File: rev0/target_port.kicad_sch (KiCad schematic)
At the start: 14 parts, among them IC1 ECP5-BGA256, U9 USB3343-CP

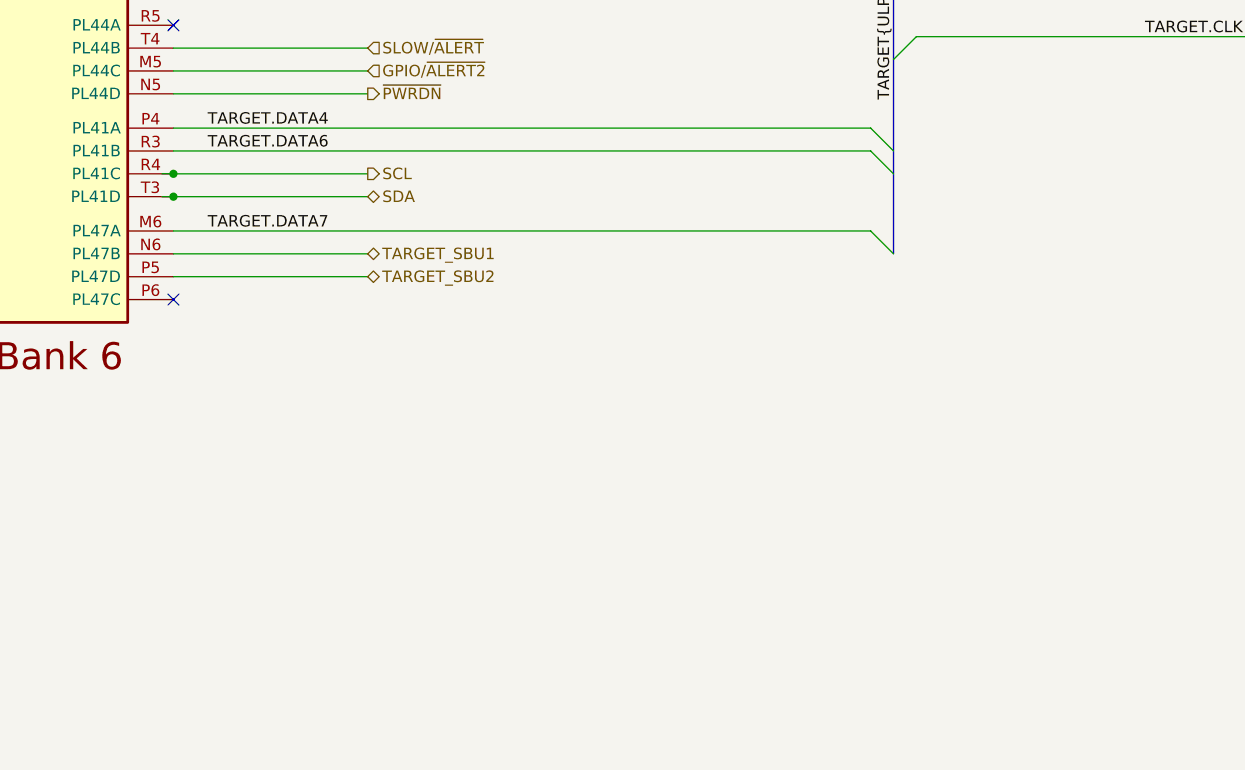
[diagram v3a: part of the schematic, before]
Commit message: hardware: add Target port Type-C controller
replaces buffers for CC pin I/O
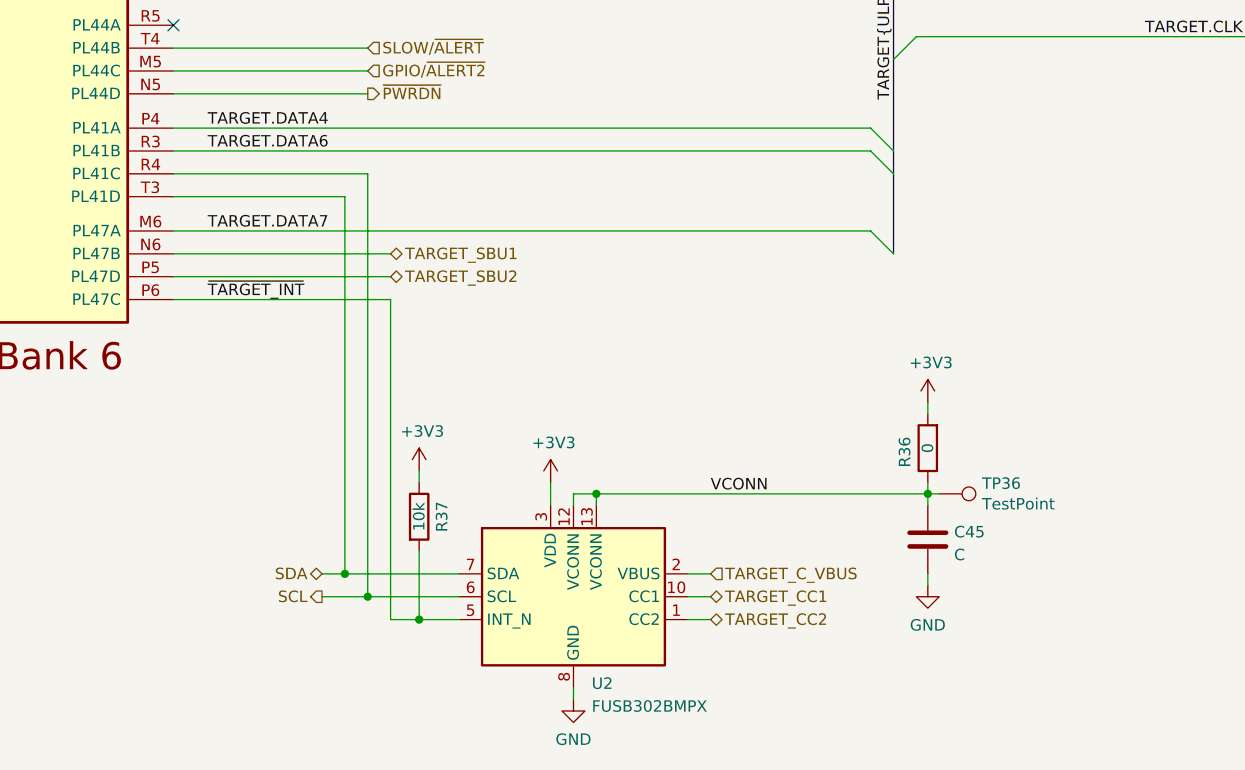
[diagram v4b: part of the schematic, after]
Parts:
- added C45: C, Capacitor_SMD:C_0402_1005Metric, symbol Device:C
- added R36: 0, Resistor_SMD:R_0402_1005Metric, symbol Device:R
- added R37: 10k, Resistor_SMD:R_0402_1005Metric, symbol Device:R
- added TP36: TestPoint, TestPoint:TestPoint_Pad_D1.0mm, symbol Connector:TestPoint
- added U2: FUSB302BMPX, Package_DFN_QFN:WQFN-14-1EP_2.5x2.5mm_P0.5mm_EP1.45x1.45mm, symbol Interface_USB:FUSB302BMPX
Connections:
- net +3V3: now also R36.2, R37.1, U2.3 (VDD), U2.4 (VDD)
- net GND: now also C45.2, U2.15 (GND), U2.8 (GND), U2.9 (GND)
- net SCL: now also U2.6 (SCL)
- net SDA: now also U2.7 (SDA)
- net TARGET_C_VBUS: now also U2.2 (VBUS)
- net ~{TARGET_INT}: now reaches IC1.P6 (PL47C)
- net ~{TARGET_INT}: now also R37.2, U2.5 (INT_N)
- new net TARGET_CC1: U2.10 (CC1), U2.11 (CC1)
- new net TARGET_CC2: U2.1 (CC2), U2.14 (CC2)
- new net VCONN: C45.1, R36.1, TP36.1, U2.12 (VCONN), U2.13 (VCONN)
- no-connect marks 8 -> 7

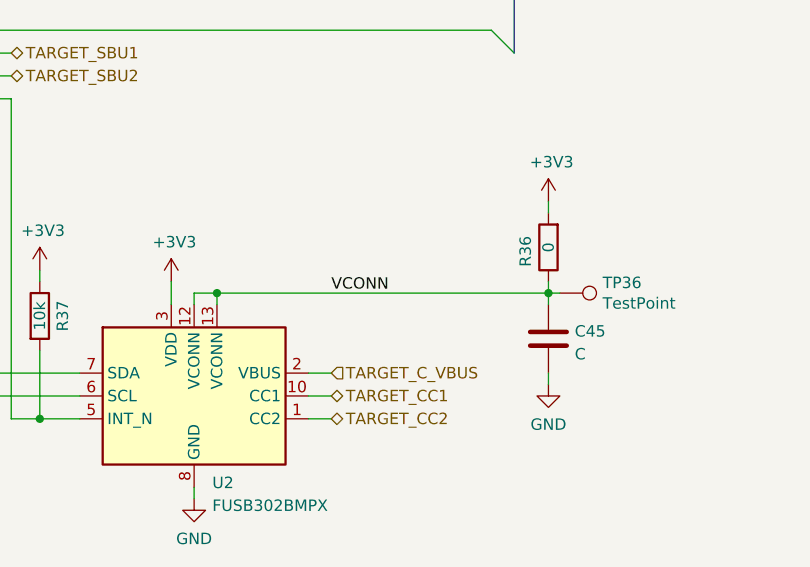
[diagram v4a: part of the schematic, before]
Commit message: hardware: add Aux port Type-C controller
replaces rudimentary CC pin input
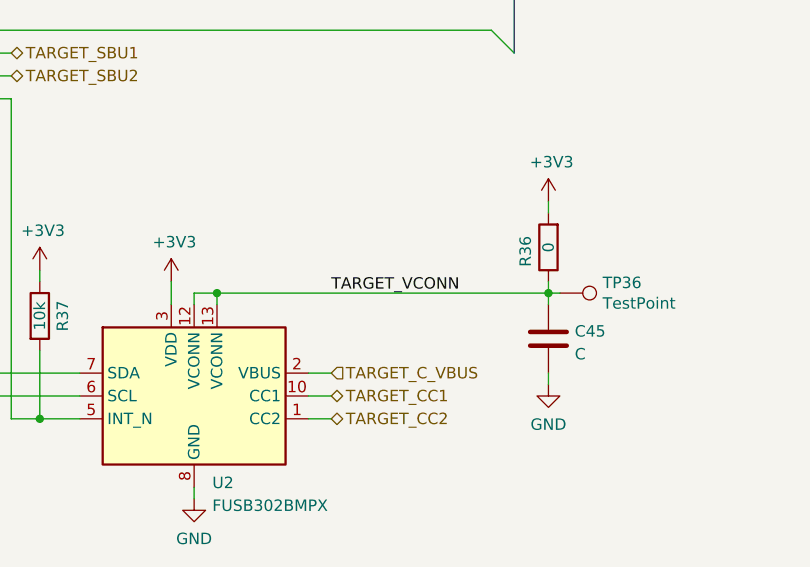
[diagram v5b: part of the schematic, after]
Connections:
- net VCONN renamed TARGET_VCONN
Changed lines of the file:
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@@
     (effects (font (size 1.27 1.27)) (justify left bottom))
   )
-  (label "VCONN" (at 119.38 165.1 0)
+  (label "TARGET_VCONN" (at 119.38 165.1 0)
     (effects (font (size 1.27 1.27)) (justify left bottom))
   )

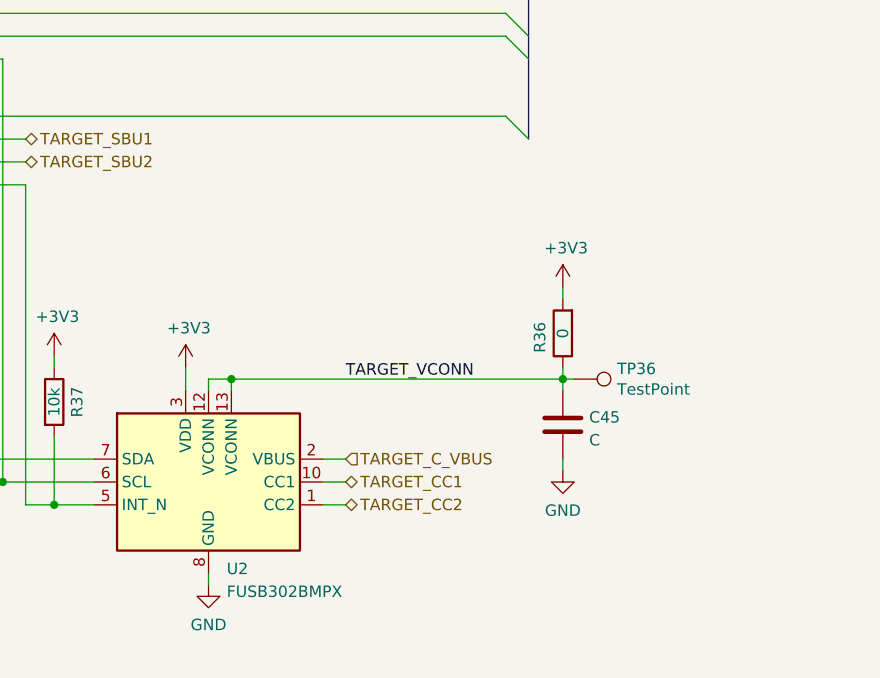
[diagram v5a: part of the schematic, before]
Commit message: hardware: simplify Control port Type-C connections
- remove CC/FPGA connections to ensure correct Rd is reliably present
- remove SBU/FPGA connections to avoid need for ESD protection

We provide CC and SBU pin access on the Target and Aux port. They are
not necessary on the Control port. Simplification ensures reliability.
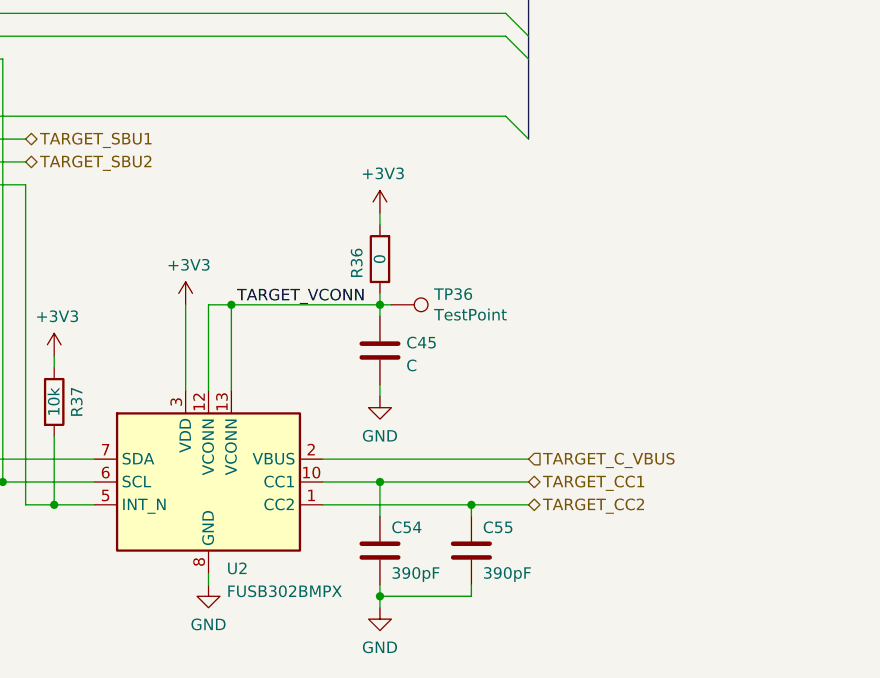
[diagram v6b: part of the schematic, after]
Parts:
- added C54, C55: 390pF, Capacitor_SMD:C_0402_1005Metric, symbol Device:C
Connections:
- net GND: now also C54.2, C55.2
- net TARGET_CC1: now also C54.1
- net TARGET_CC2: now also C55.1
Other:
- moved on the sheet: C45, R36, TP36

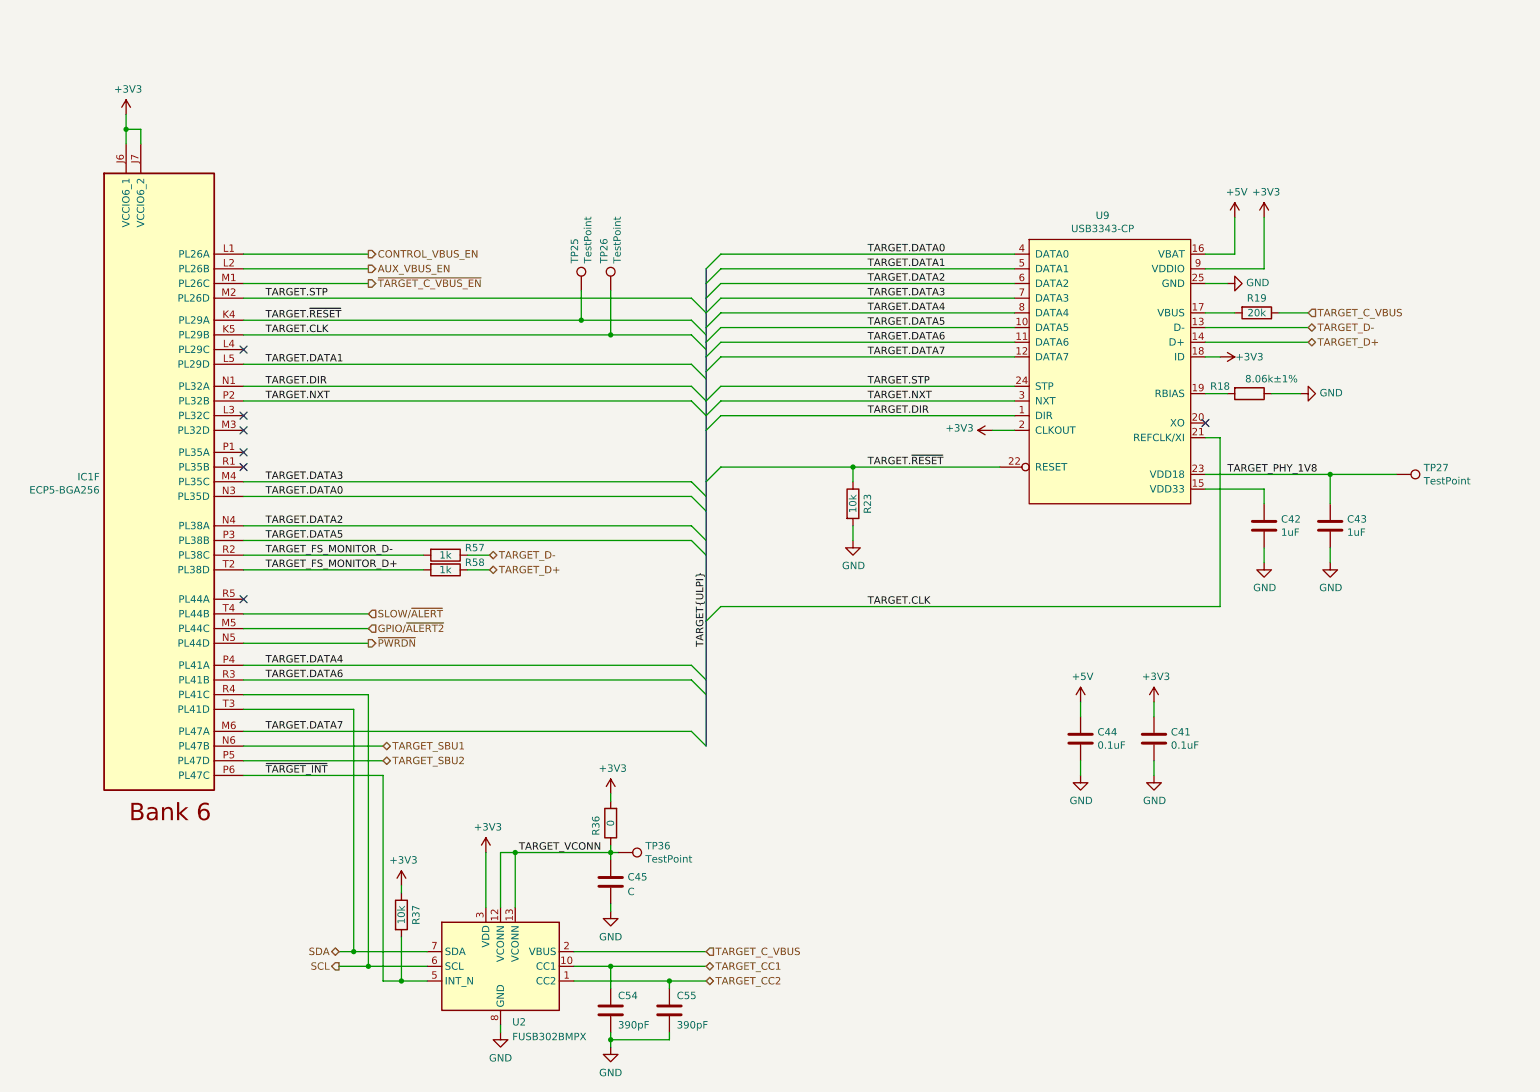
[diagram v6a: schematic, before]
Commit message: hardware: clamp VBUS detection signals to 24 V
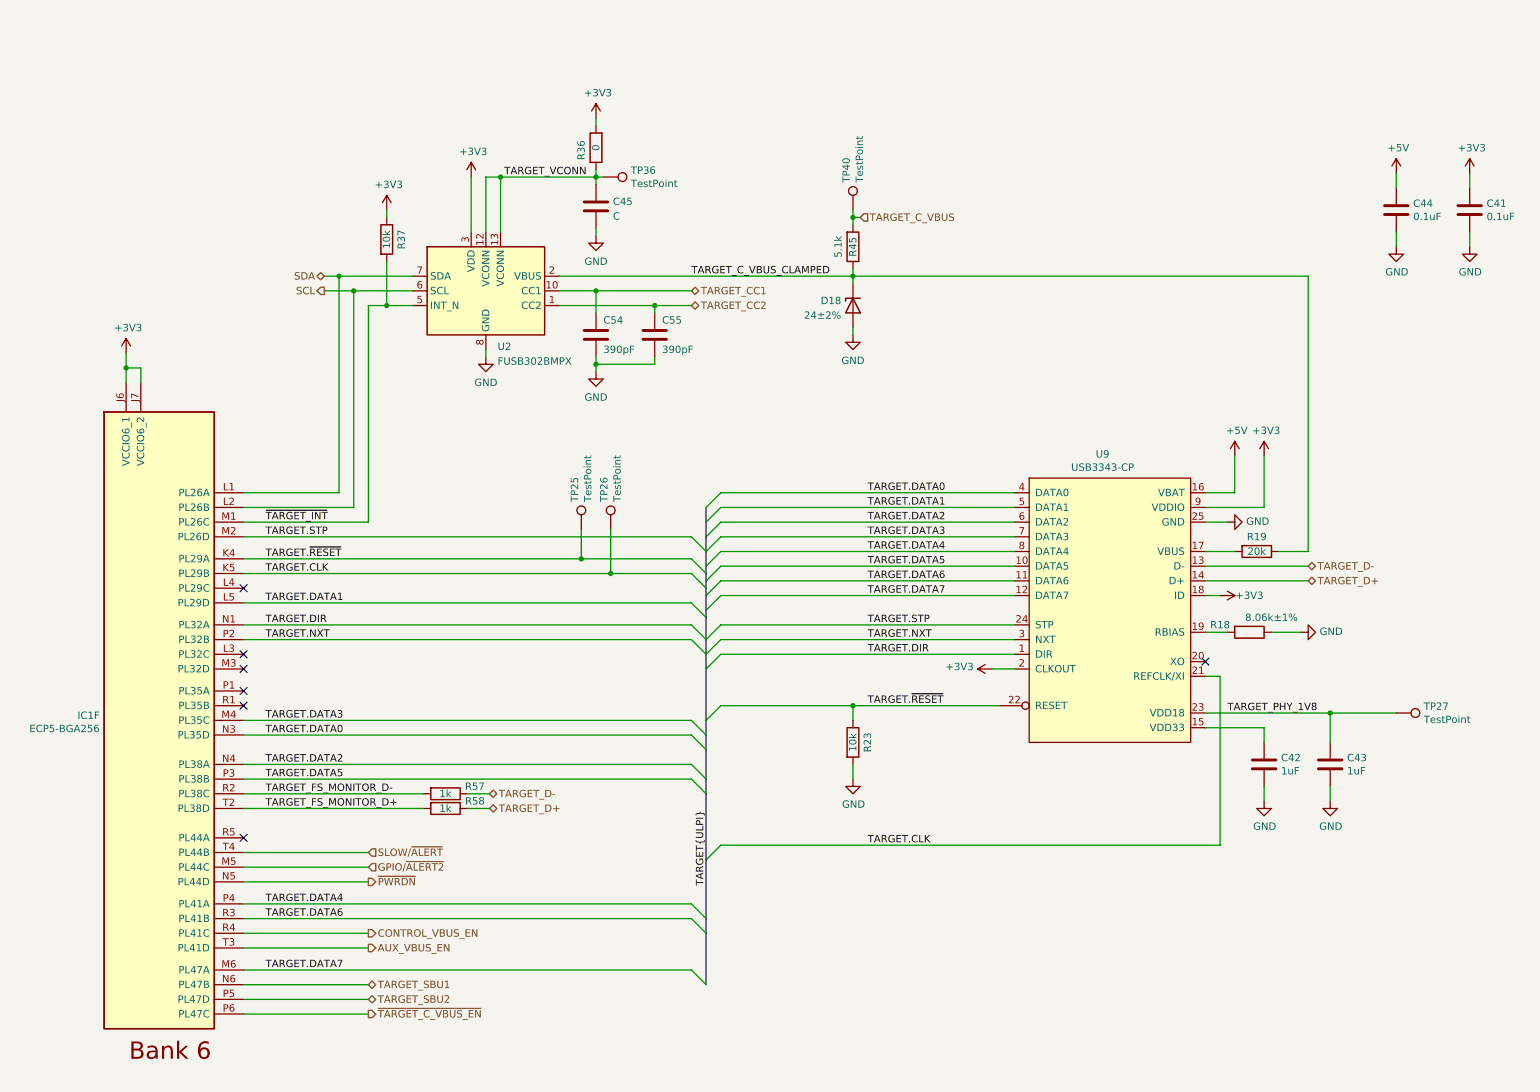
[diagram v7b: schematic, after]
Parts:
- added D18: 24±2%, luna:DFN1006-2, symbol Device:D_Zener
- added R45: 5.1k, Resistor_SMD:R_0402_1005Metric, symbol Device:R
- added TP40: TestPoint, TestPoint:TestPoint_Pad_D1.0mm, symbol Connector:TestPoint
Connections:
- net AUX_VBUS_EN: now also IC1.T3 (PL41D); no longer IC1.L2 (PL26B)
- net CONTROL_VBUS_EN: now also IC1.R4 (PL41C); no longer IC1.L1 (PL26A)
- net GND: now also D18.2 (A)
- net SCL: now also IC1.L2 (PL26B); no longer IC1.R4 (PL41C)
- net SDA: now also IC1.L1 (PL26A); no longer IC1.T3 (PL41D)
- net TARGET_C_VBUS: now also R45.2, TP40.1; no longer R19.1, U2.2 (VBUS)
- net ~{TARGET_C_VBUS_EN}: now also IC1.P6 (PL47C); no longer IC1.M1 (PL26C)
- net ~{TARGET_INT}: now also IC1.M1 (PL26C); no longer IC1.P6 (PL47C)
- new net TARGET_C_VBUS_CLAMPED: D18.1 (K), R19.1, R45.1, U2.2 (VBUS)
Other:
- moved on the sheet: C41, C42, C43, C44, C45, C54, C55, IC1F, R18, R19, R23, R36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

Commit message: hardware: protect CC and SBU pins
add overvoltage and ESD protection for Aux port and Target port USB
Type-C CC and SBU pins
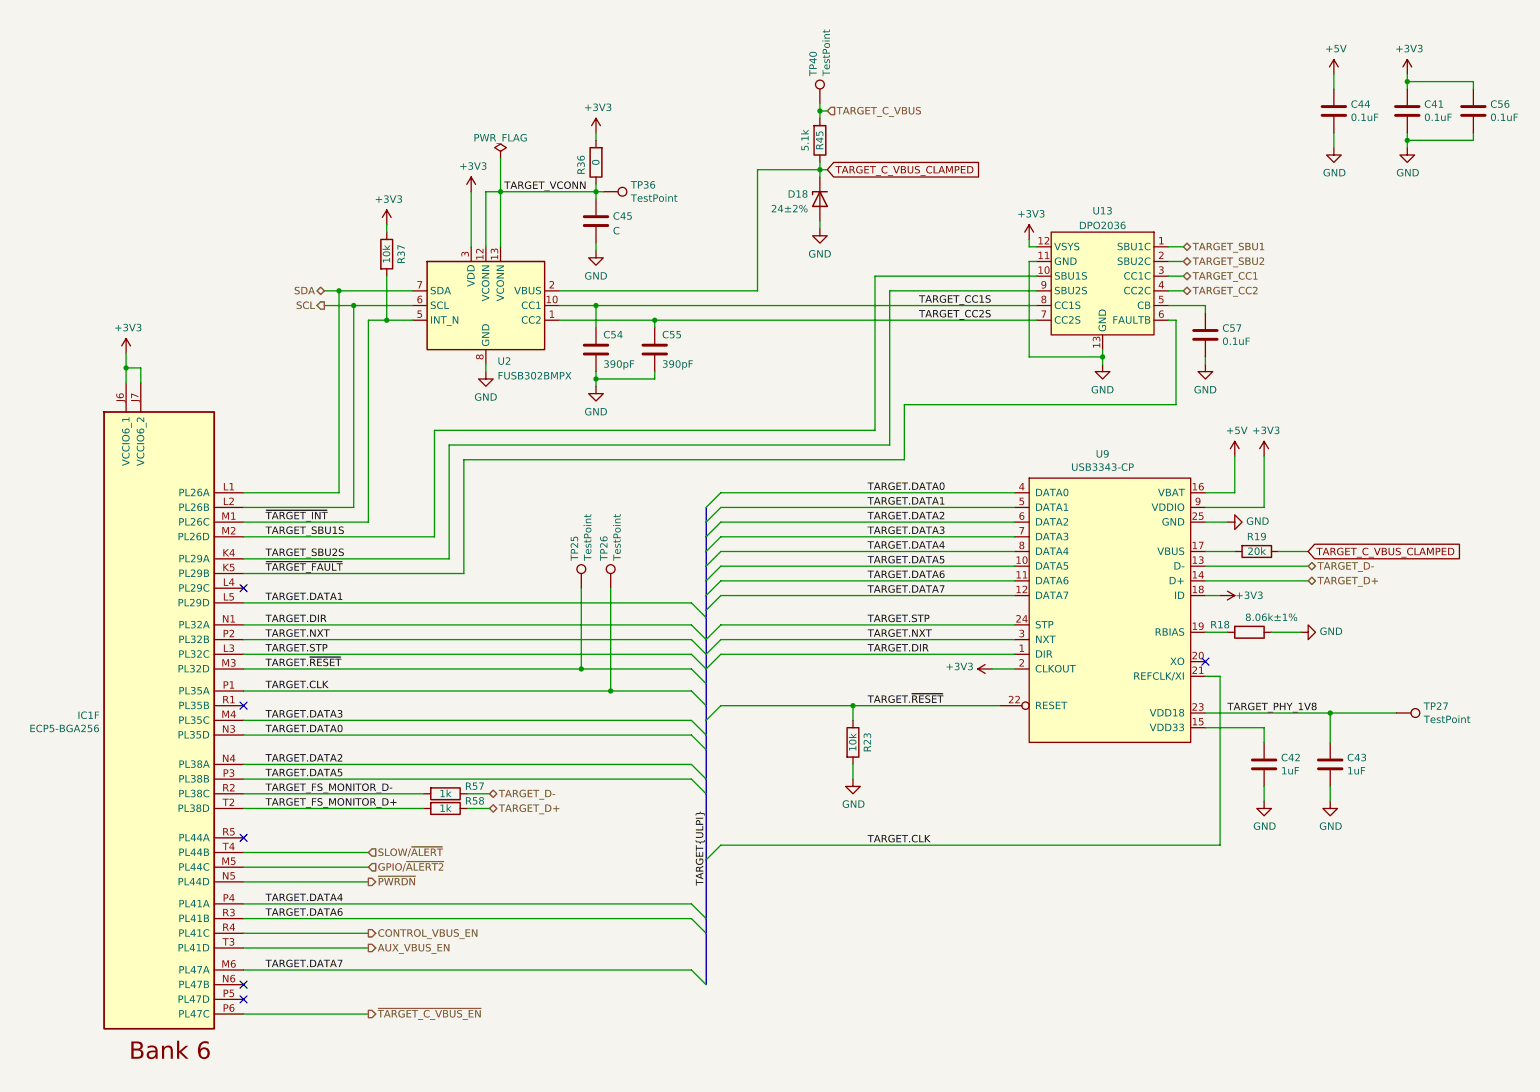
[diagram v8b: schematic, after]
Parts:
- added C56, C57: 0.1uF, Capacitor_SMD:C_0402_1005Metric, symbol Device:C
- added U13: DPO2036, luna:Diodes_UQFN2020-12_Type-B, symbol usb:DPO2036
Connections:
- net +3V3: now also C56.1, U13.12 (VSYS)
- net GND: now also C56.2, C57.2, U13.11 (GND), U13.13 (GND)
- net TARGET.CLK: now also IC1.P1 (PL35A); no longer IC1.K5 (PL29B)
- net TARGET.STP: now also IC1.L3 (PL32C); no longer IC1.M2 (PL26D)
- net TARGET.~{RESET}: now also IC1.M3 (PL32D); no longer IC1.K4 (PL29A)
- net TARGET_CC1: now also U13.3 (CC1C); no longer C54.1, U2.10 (CC1), U2.11 (CC1)
- net TARGET_CC2: now also U13.4 (CC2C); no longer C55.1, U2.1 (CC2), U2.14 (CC2)
- net TARGET_SBU1: now also U13.1 (SBU1C); no longer IC1.N6 (PL47B)
- net TARGET_SBU2: now also U13.2 (SBU2C); no longer IC1.P5 (PL47D)
- new net: C57.1, U13.5 (CB)
- new net TARGET_CC1S: C54.1, U13.8 (CC1S), U2.10 (CC1), U2.11 (CC1)
- new net TARGET_CC2S: C55.1, U13.7 (CC2S), U2.1 (CC2), U2.14 (CC2)
- new net TARGET_SBU1S: IC1.M2 (PL26D), U13.10 (SBU1S)
- new net TARGET_SBU2S: IC1.K4 (PL29A), U13.9 (SBU2S)
- new net ~{TARGET_FAULT}: IC1.K5 (PL29B), U13.6 (FAULTB)
- no-connect marks 7 -> 6
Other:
- moved on the sheet: C41, C44, C45, C54, C55, D18, R36, R37, R45, TP25, TP26, TP36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
